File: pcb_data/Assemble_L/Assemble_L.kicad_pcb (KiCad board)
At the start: 2 copper layers, 159.5 x 95.2 mm, 75 parts, among them U1 XIAO-nRF52840

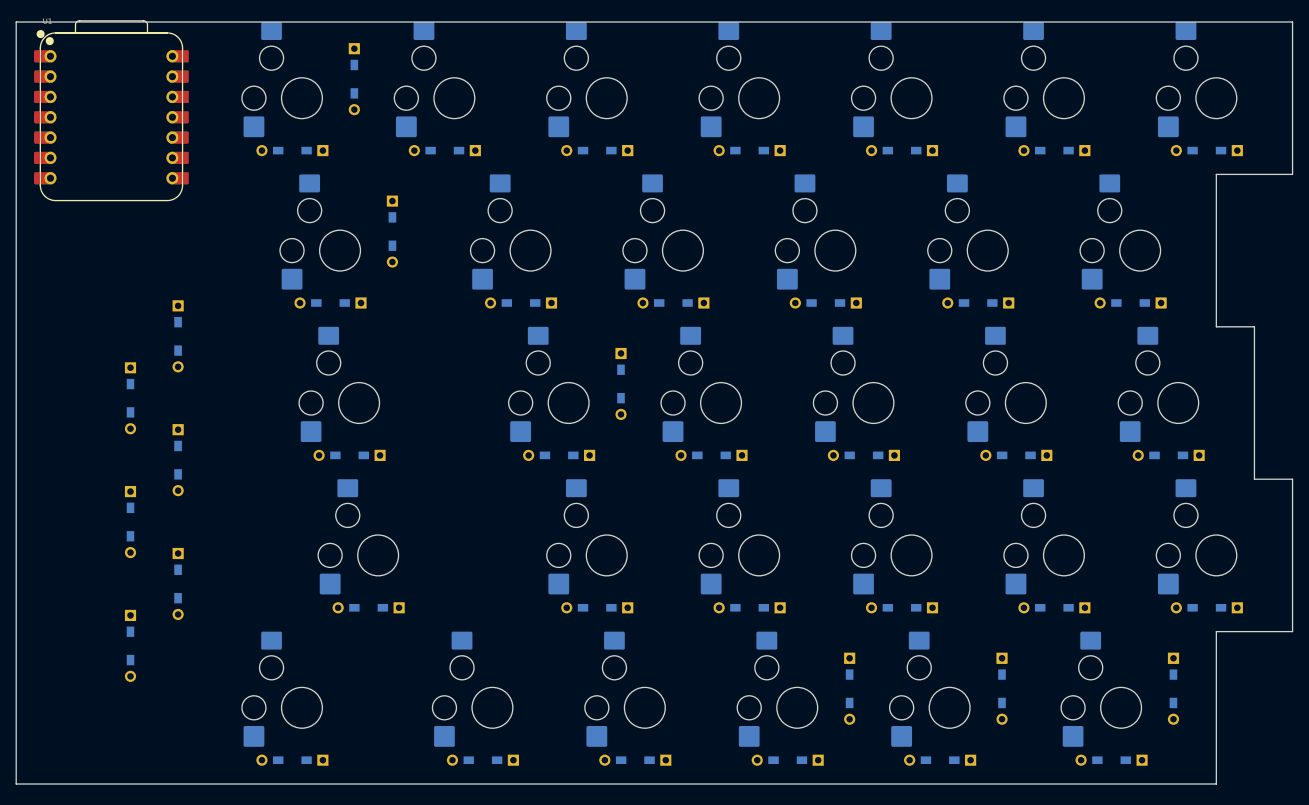
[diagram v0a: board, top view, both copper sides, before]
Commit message: complete to design pattern of board L
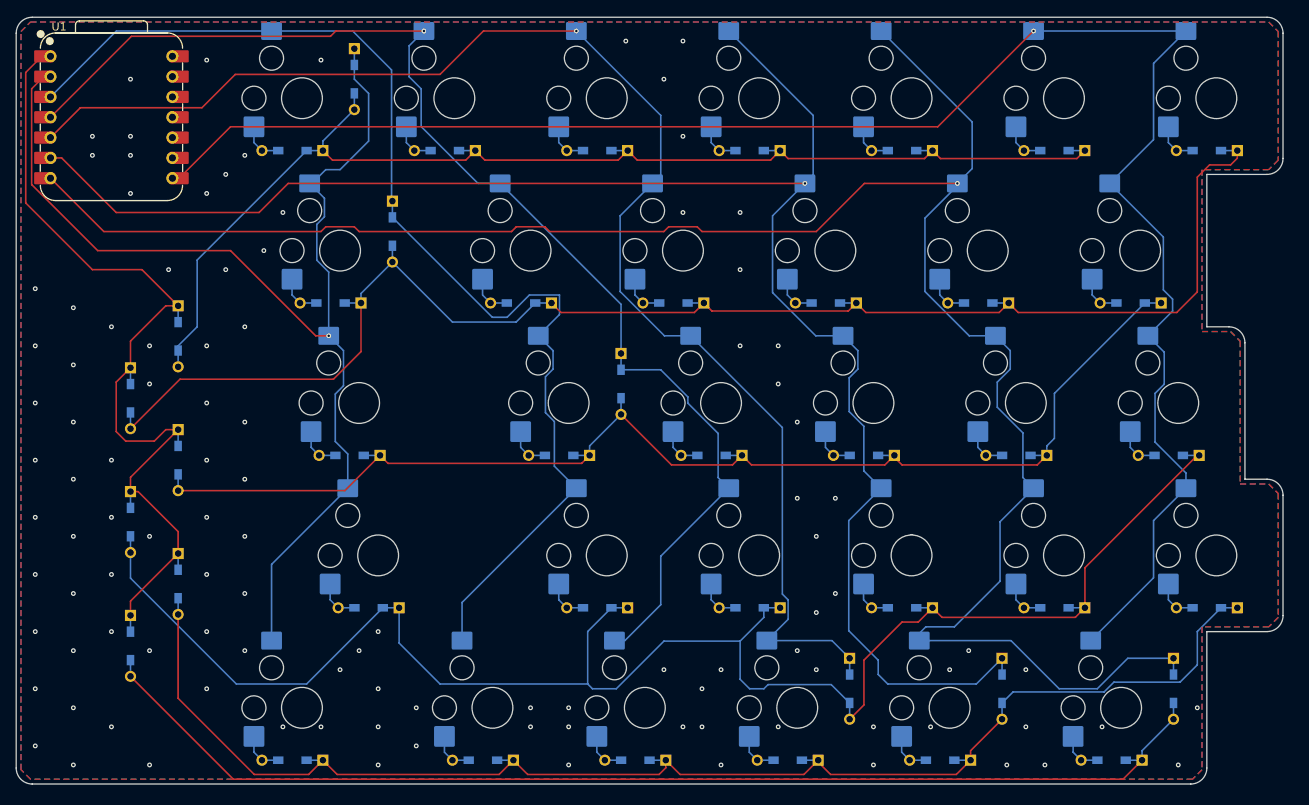
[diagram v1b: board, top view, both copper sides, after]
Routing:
- net IO 5: track 0.00 -> 259.5 mm, vias 0 -> 1
- net IO 6: track 0.00 -> 226.0 mm, vias 0 -> 1
- net IO 4: track 0.00 -> 216.6 mm, vias 0 -> 1
- net Net-(D0-3-K): track 0.00 -> 213.1 mm
- net Net-(D0-1-K): track 0.00 -> 190.7 mm
- net IO 3: track 0.00 -> 178.9 mm, vias 0 -> 1
- net Net-(D0-4-K): track 0.00 -> 178.6 mm
- net Net-(D0-2-K): track 0.00 -> 159.7 mm
- net IO 2: track 0.00 -> 155.9 mm, vias 0 -> 1
- net Net-(D1-0-K): track 0.00 -> 154.5 mm
- net IO 1: track 0.00 -> 146.7 mm
- net IO 0: track 0.00 -> 145.6 mm, vias 0 -> 1
- net Net-(D6-5-K): track 0.00 -> 145.6 mm
- net INTR_L: track 0.00 -> 116.7 mm
- net Net-(D3-0-A): track 0.00 -> 6.84 mm
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- added copper zone on B.Cu, net GND
- added copper zone on F.Cu, net GND
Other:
- board size 159.5 x 95.2 mm -> 158.4 x 95.8 mm

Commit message: fix line width 0.2 -> 0.5
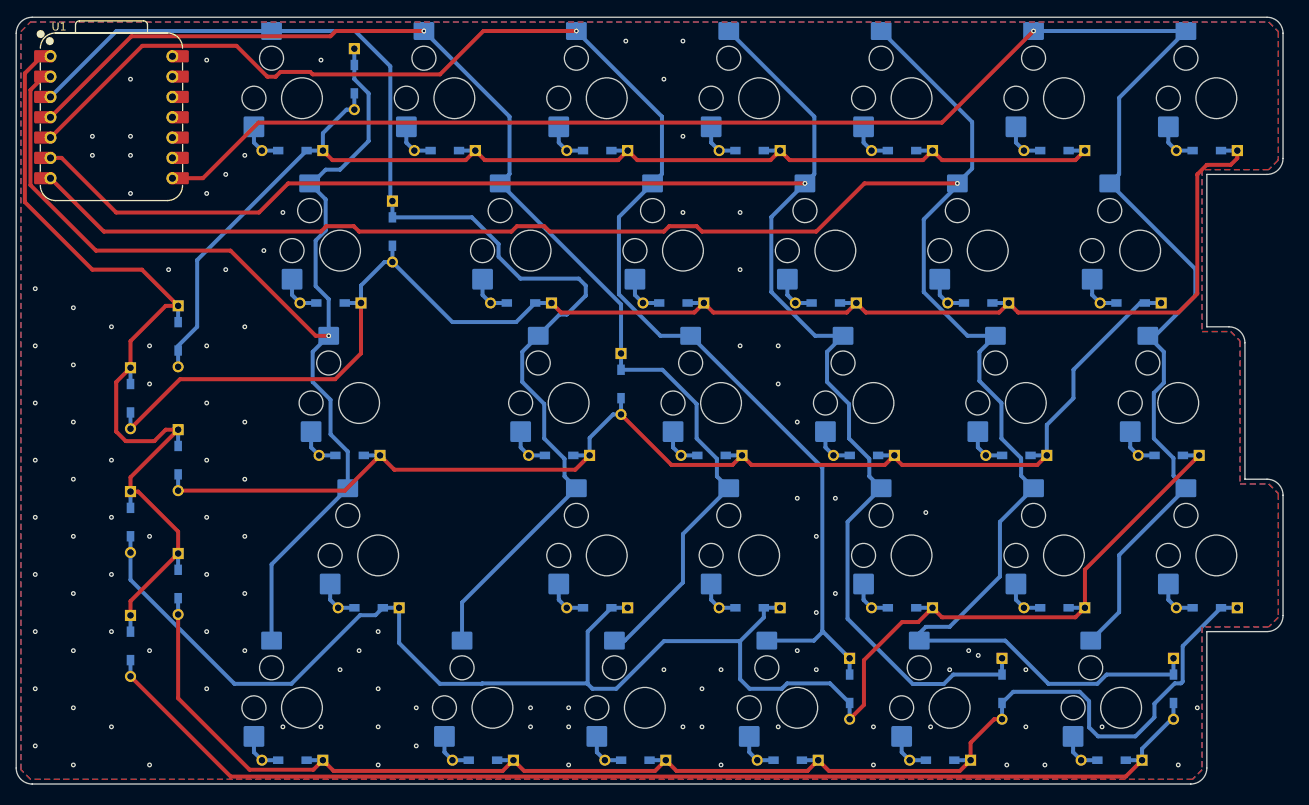
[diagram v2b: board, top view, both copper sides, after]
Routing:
- net Net-(D0-4-K): track 178.6 -> 184.5 mm
- net IO 1: track 146.7 -> 152.3 mm
- net IO 3: track 178.9 -> 183.4 mm
- net IO 6: track 226.0 -> 229.0 mm
- net IO 5: track 259.5 -> 257.3 mm
- net IO 2: track 155.9 -> 153.8 mm
- net Net-(D0-2-K): track 159.7 -> 161.3 mm
- net IO 4: track 216.6 -> 215.1 mm
- net IO 0: track 145.6 -> 147.0 mm
- net Net-(D0-1-K): track 190.7 -> 191.9 mm
- net Net-(D1-0-K): track 154.5 -> 155.4 mm
- net GND: vias 109 -> 110

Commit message: add GND plane
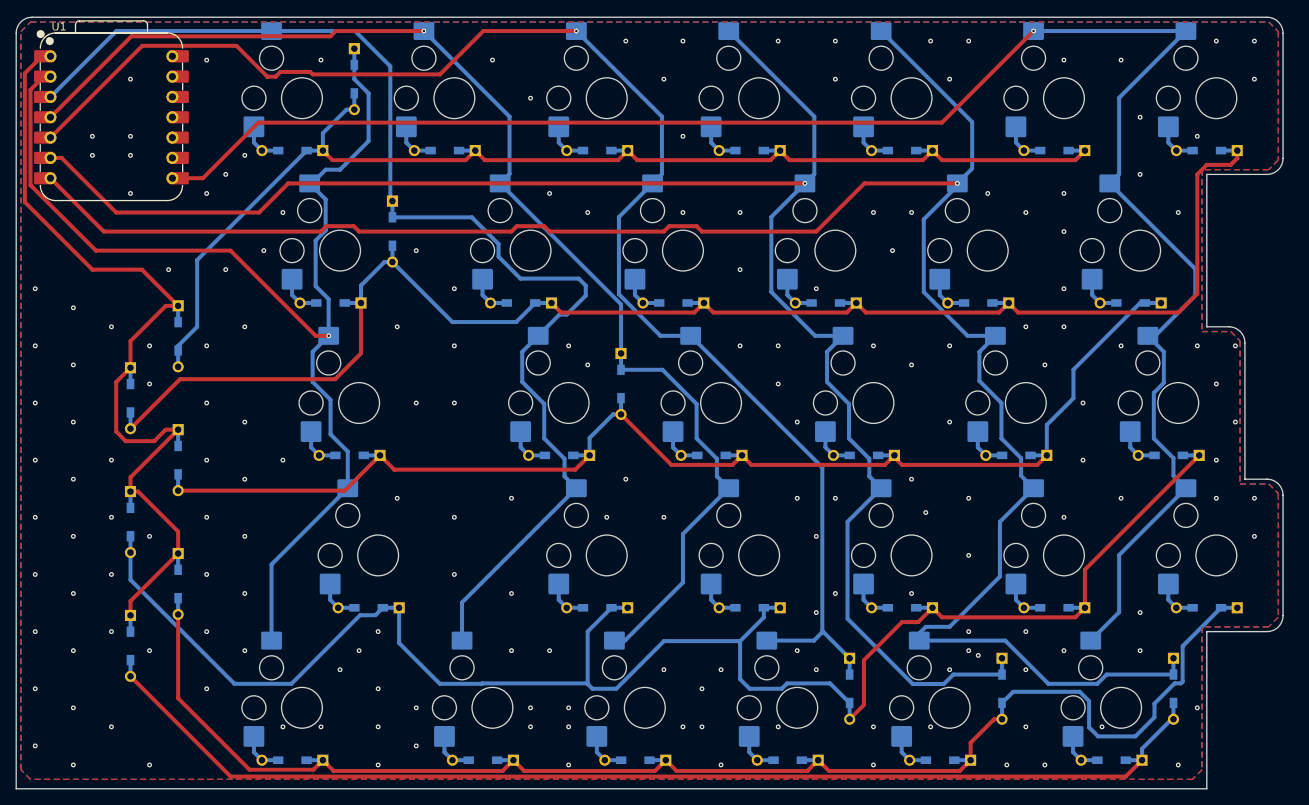
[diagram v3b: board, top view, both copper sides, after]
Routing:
- net GND: vias 110 -> 186
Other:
- board size 158.4 x 95.8 mm -> 158.4 x 96.4 mm

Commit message: add mount hole (#5)
ネジ穴を追加しました．
特にレビュー項目はない（git logを綺麗に残すためのPR）のでセルフマージします．
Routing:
- net Net-(D0-4-K): track 184.5 -> 185.1 mm
- net GND: vias 186 -> 187
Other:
- outline, holes or cut-outs redrawn

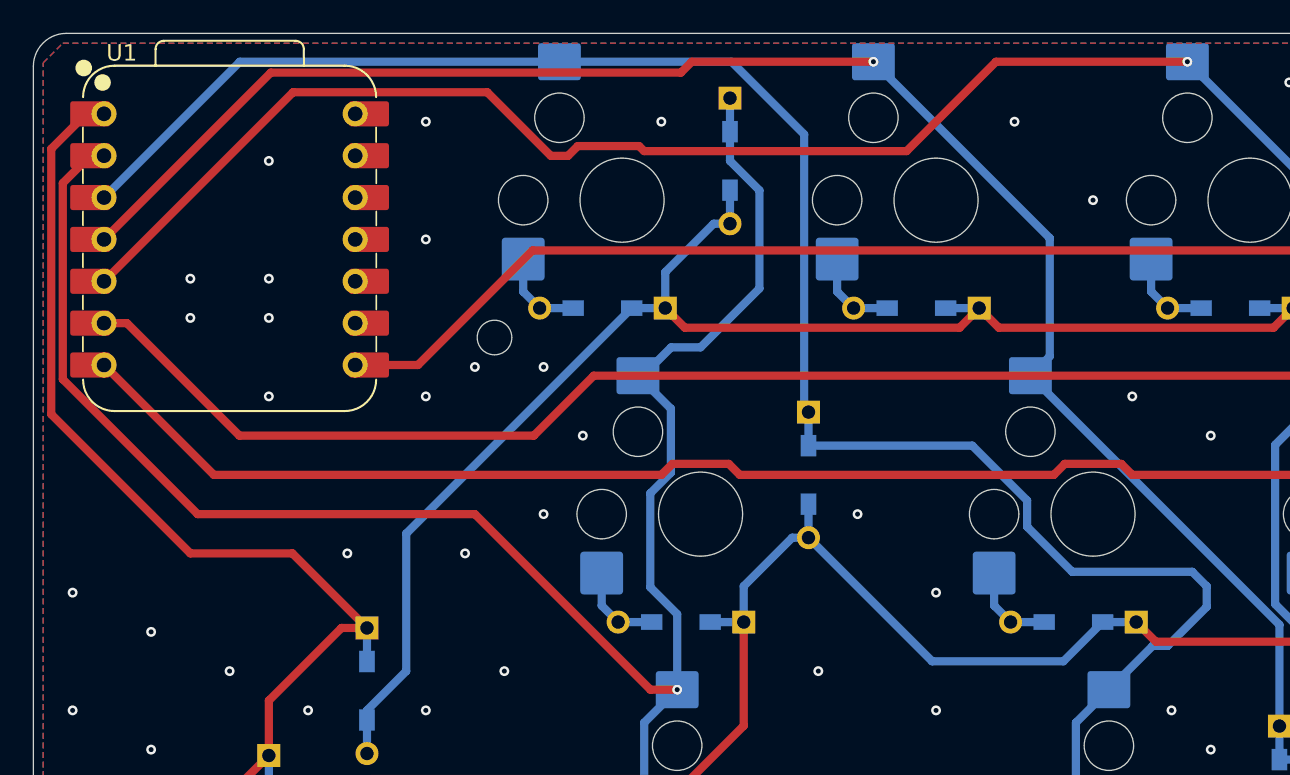
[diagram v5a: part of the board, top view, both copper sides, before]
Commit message: apply footprint update, and fix patterns
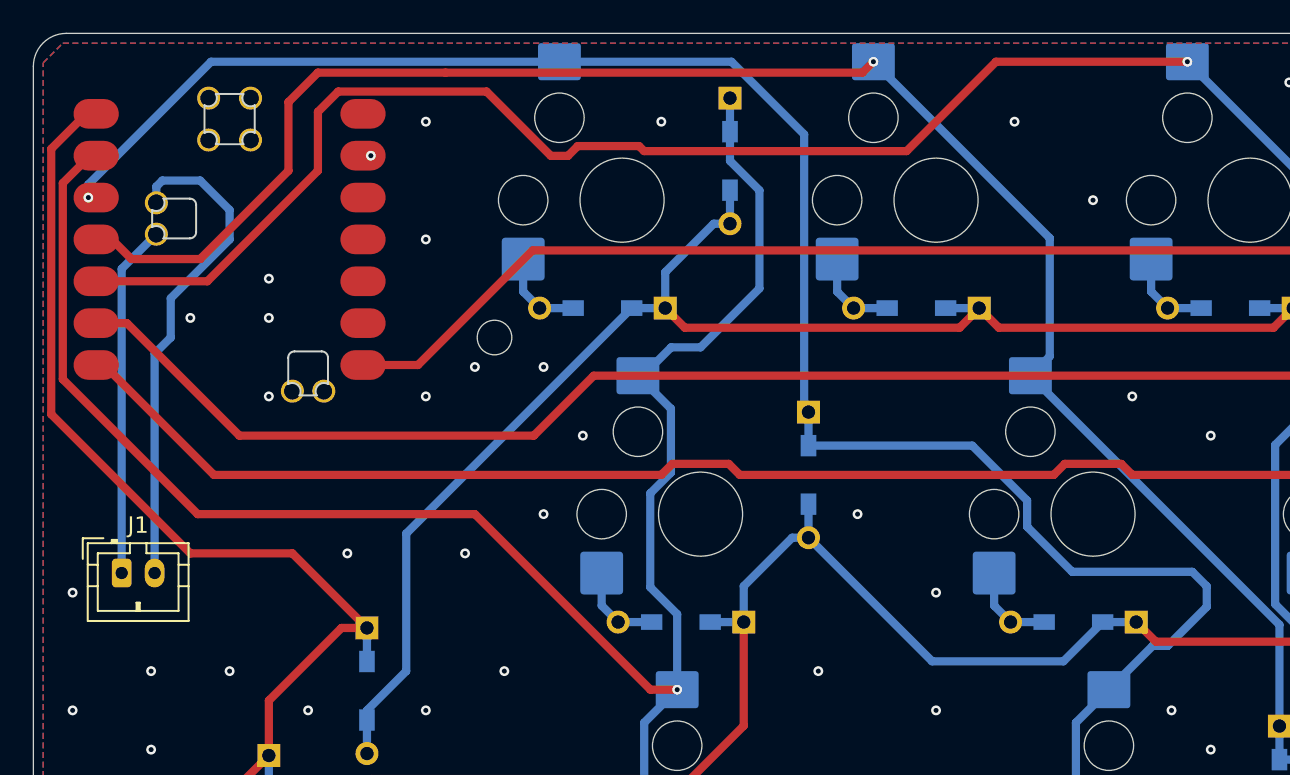
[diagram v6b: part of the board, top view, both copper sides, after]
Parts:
- added J1: Conn_01x02, Connector_JST:JST_PH_B2B-PH-K_1x02_P2.00mm_Vertical, F.Cu at (50.6, 79.8)
- U1: footprint Seeed Studio XIAO Series Library:XIAO-nRF52840-DIP -> mcu:xiao-ble-smd-cutout
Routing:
- net GND: track 0.00 -> 30.2 mm, vias 187 -> 186
- net BAT+: track 0.00 -> 21.4 mm
- net IO 2: track 153.8 -> 158.2 mm
- net IO 3: track 183.4 -> 186.5 mm
- net IO 1: track 152.3 -> 153.7 mm, vias 0 -> 1

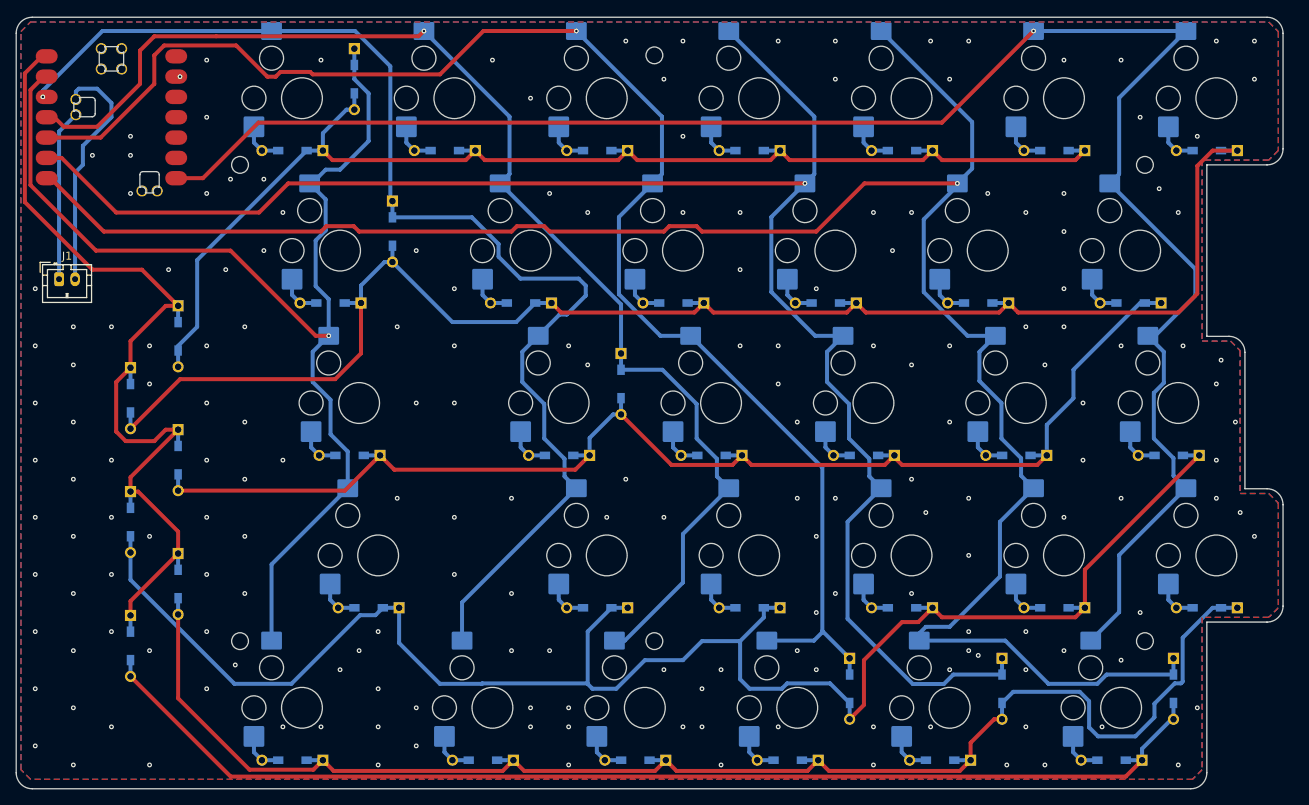
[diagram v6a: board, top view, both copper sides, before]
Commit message: add mount hole, and fix patterns
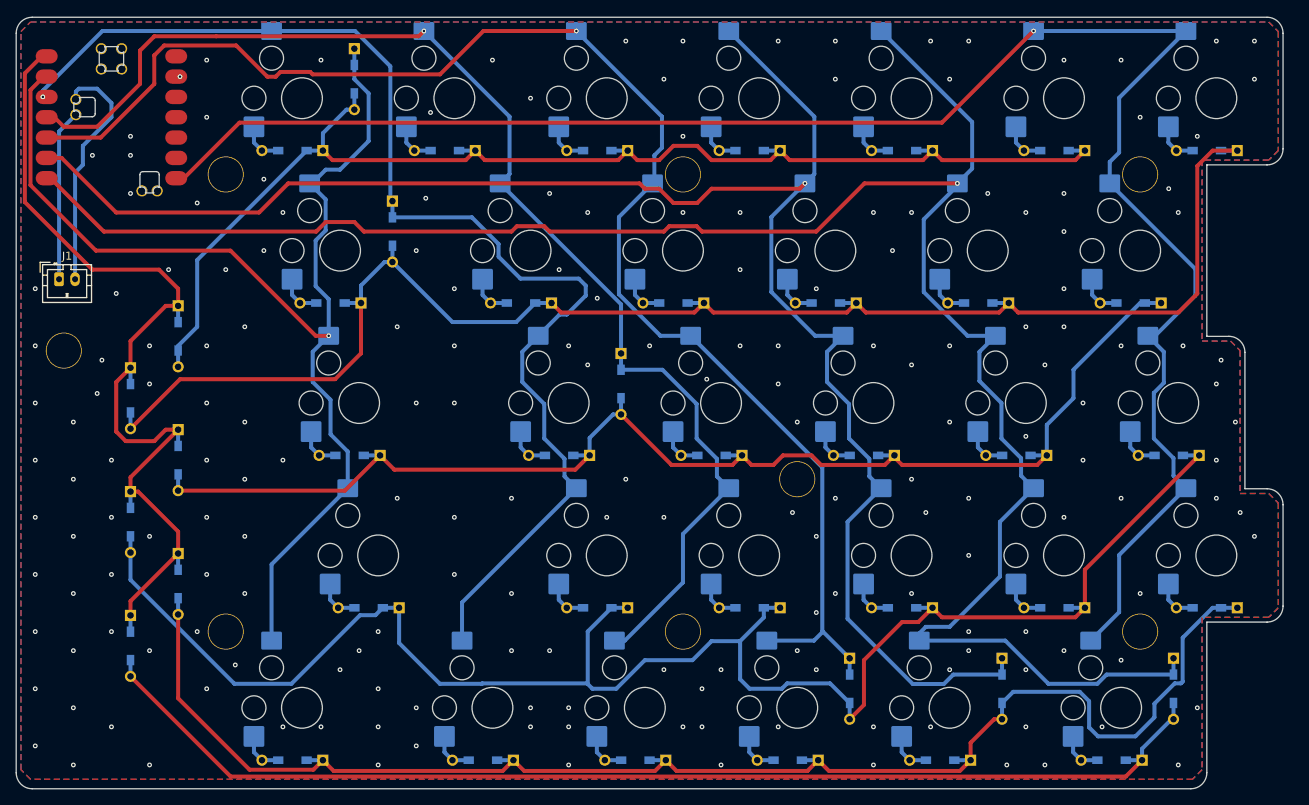
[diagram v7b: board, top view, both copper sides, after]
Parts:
- added H1: MountingHole, kbd_Hole:m2_Spacer_Hole, F.Cu at (71.4, 66.7)
- added H2: MountingHole, kbd_Hole:m2_Spacer_Hole, F.Cu at (128.6, 66.7)
- added H3: MountingHole, kbd_Hole:m2_Spacer_Hole, F.Cu at (185.7, 66.7)
- added H4: MountingHole, kbd_Hole:m2_Spacer_Hole, F.Cu at (71.4, 123.8)
- added H5: MountingHole, kbd_Hole:m2_Spacer_Hole, F.Cu at (128.6, 123.8)
- added H6: MountingHole, kbd_Hole:m2_Spacer_Hole, F.Cu at (185.7, 123.8)
- added H7: MountingHole, kbd_Hole:m2_Spacer_Hole, F.Cu at (51.2, 88.7)
- added H8: MountingHole, kbd_Hole:m2_Spacer_Hole, F.Cu at (142.9, 104.8)
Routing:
- net IO 4: track 215.1 -> 217.1 mm
- net Net-(D1-0-K): track 155.4 -> 156.9 mm
- net INTR_L: track 116.7 -> 118.0 mm
- net Net-(D0-2-K): track 161.3 -> 162.2 mm
- net GND: vias 186 -> 192
- net (no net): vias 1 -> 0
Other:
- outline, holes or cut-outs redrawn
